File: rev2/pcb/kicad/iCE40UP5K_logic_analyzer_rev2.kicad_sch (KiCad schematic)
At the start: 155 parts, among them IC1 ICE40UP5K-SG48I, IC2 MIC5504-3.3YM5-TR, IC3 MIC5504-1.2YM5-TR, IC4 FT2232HL-TRAY, IC5 W25Q40CLSNIG, IC6 SN74LVC14ADBRE4, IC7 SN74LVC14ADBRE4, IC8 SN74LVC14ADBRE4, J1 USB B Female Connector, J2 61300611121, J3 61202021621, J4 61300821121, J5 61300821121, J6 61300311121, J7 61300621121, Q1 2N7002H6327XTSA2, Y1 830208214809

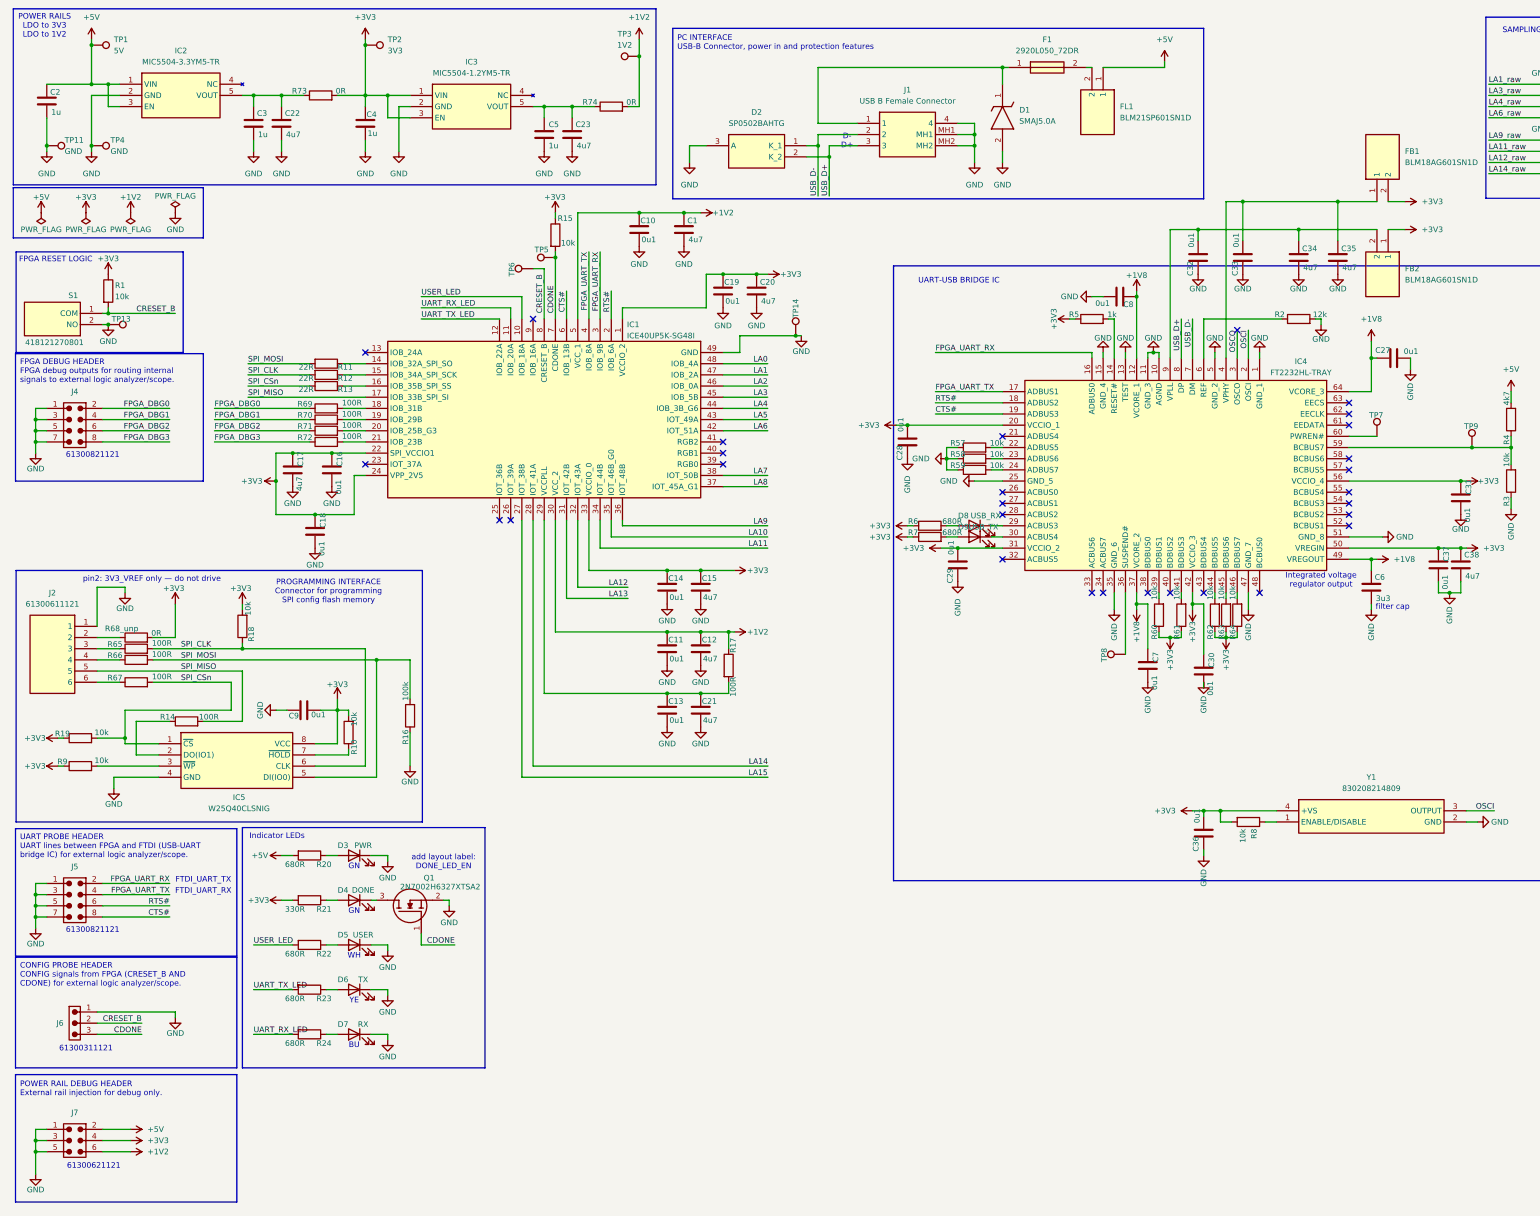
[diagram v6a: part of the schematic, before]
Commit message: reworked schematic test pads. Cleaned up multiple of the schematic blocks.
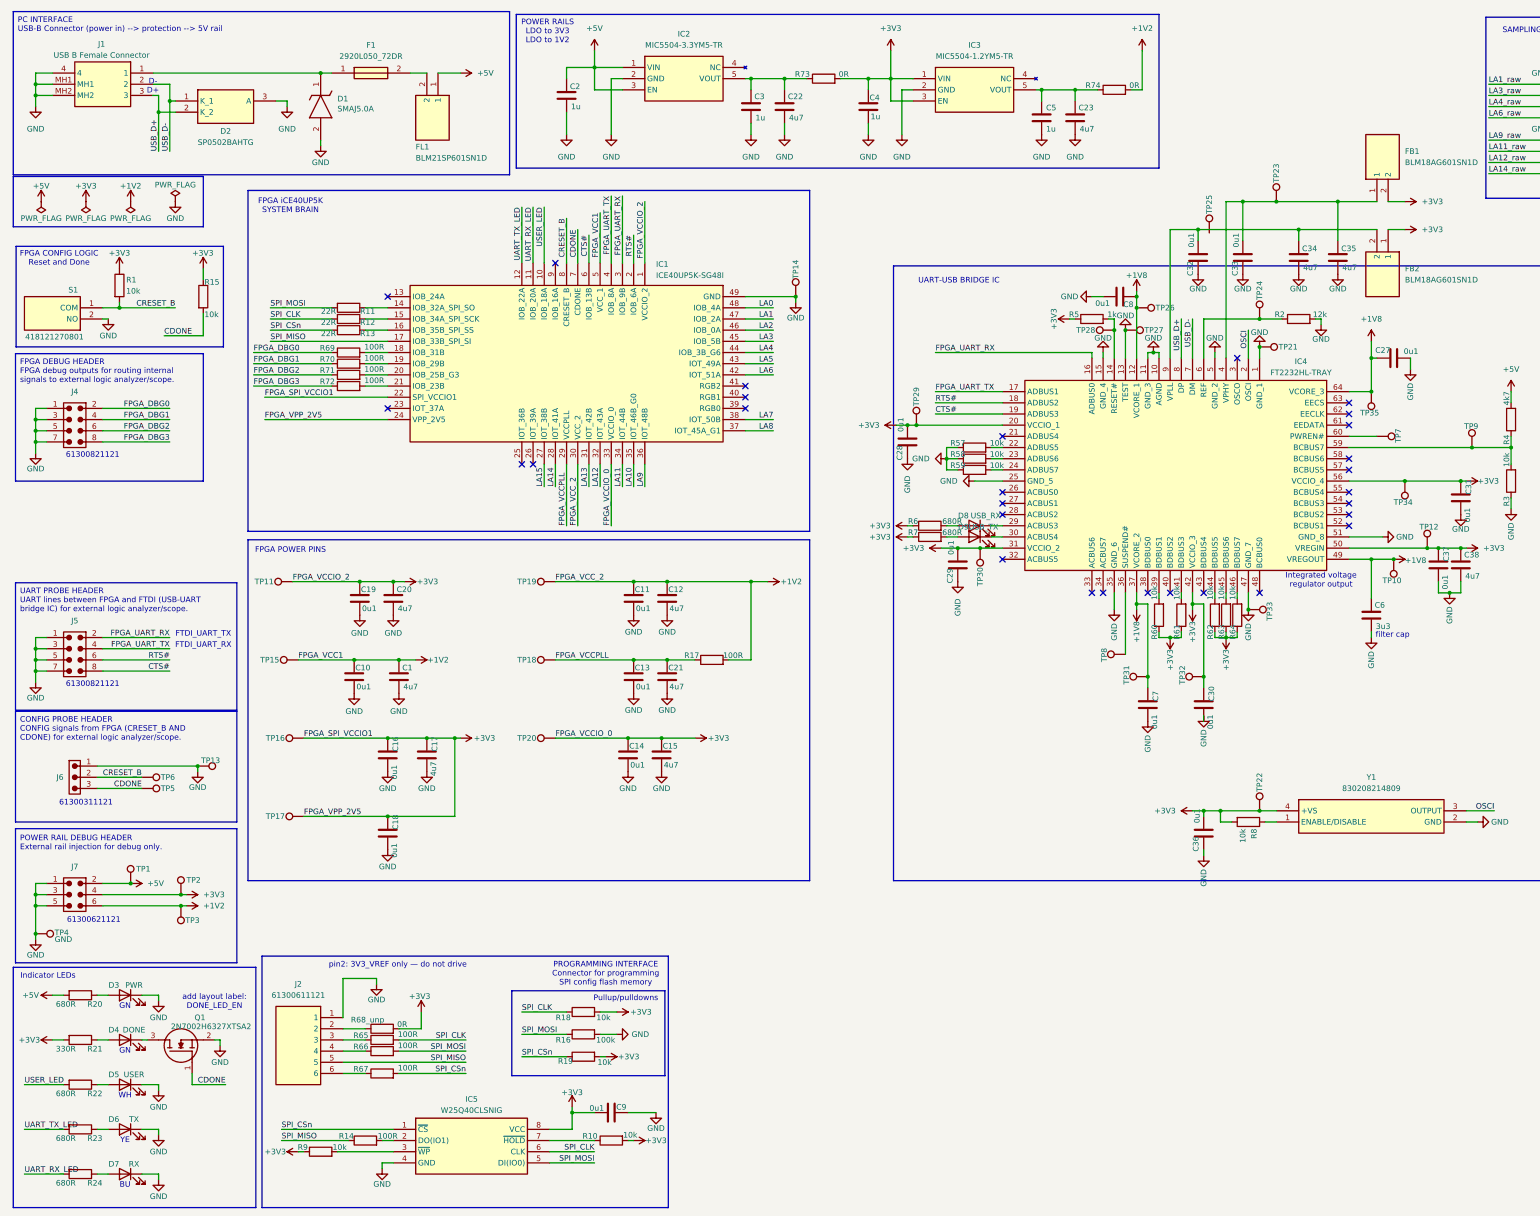
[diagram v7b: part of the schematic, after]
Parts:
- added TP10: VREGOUT, TestPoint:TestPoint_Pad_D1.0mm, symbol Connector:TestPoint
- added TP12: VREGIN, TestPoint:TestPoint_Pad_D1.0mm, symbol Connector:TestPoint
- added TP15: VCC1, TestPoint:TestPoint_Pad_D1.0mm, symbol Connector:TestPoint
- added TP16: SPI_VCCIO1, TestPoint:TestPoint_Pad_D1.0mm, symbol Connector:TestPoint
- added TP17: VPP_2V5, TestPoint:TestPoint_Pad_D1.0mm, symbol Connector:TestPoint
- added TP18: VCC_PLL, TestPoint:TestPoint_Pad_D1.0mm, symbol Connector:TestPoint
- added TP19: VCC_2, TestPoint:TestPoint_Pad_D1.0mm, symbol Connector:TestPoint
- added TP20: VCCIO_0, TestPoint:TestPoint_Pad_D1.0mm, symbol Connector:TestPoint
- added TP21, TP33: GND, TestPoint:TestPoint_Pad_D1.0mm, symbol Connector:TestPoint
- added TP22: VS_OSC, TestPoint:TestPoint_Pad_D1.0mm, symbol Connector:TestPoint
- added TP23: VPHY, TestPoint:TestPoint_Pad_D1.0mm, symbol Connector:TestPoint
- added TP24: REF, TestPoint:TestPoint_Pad_D1.0mm, symbol Connector:TestPoint
- added TP25, TP29, TP30: VPLL, TestPoint:TestPoint_Pad_D1.0mm, symbol Connector:TestPoint
- added TP26: VCORE_1, TestPoint:TestPoint_Pad_D1.0mm, symbol Connector:TestPoint
- added TP27: TEST, TestPoint:TestPoint_Pad_D1.0mm, symbol Connector:TestPoint
- added TP28: RESET#, TestPoint:TestPoint_Pad_D1.0mm, symbol Connector:TestPoint
- added TP31: VCORE_2, TestPoint:TestPoint_Pad_D1.0mm, symbol Connector:TestPoint
- added TP32: VCCIO_3, TestPoint:TestPoint_Pad_D1.0mm, symbol Connector:TestPoint
- added TP34: VCCIO_4, TestPoint:TestPoint_Pad_D1.0mm, symbol Connector:TestPoint
- added TP35: PWREN#, TestPoint:TestPoint_Pad_D1.0mm, symbol Connector:TestPoint
- TP11: value GND -> VCCIO_2; footprint TestPoint:TestPoint_Pad_D1.5mm -> TestPoint:TestPoint_Pad_D1.0mm
- TP7: value BRIDGE_PWREN# -> PWREN#
- TP8: value BRIDGE_SUSPEND# -> SUSPEND#
- TP9: value BRIDGE_PWRSAV# -> PWRSAV#
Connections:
- net +1V2: now also R17.2, TP15.1, TP19.1; no longer R17.1
- net +1V8: now also TP10.1, TP26.1, TP31.1, TP35.1
- net +3V3: now also R19.2, TP11.1, TP12.1, TP16.1, TP17.1, TP20.1, TP22.1, TP29.1, TP30.1, TP32.1, TP34.1; no longer R19.1
- net GND: now also R16.2, TP21.1, TP27.1, TP33.1; no longer R16.1, TP11.1
- net LA14: now also IC1.28 (IOT_41A)
- net LA15: now also IC1.27 (IOT_38B)
- net SPI_CSn: now also R19.1; no longer R19.2
- net SPI_MISO: now also R14.1; no longer R14.2
- net SPI_MOSI: now also R16.1; no longer R16.2
- net FPGA_VCCPLL: now reaches C13.1, C21.1, IC1.29 (VCCPLL)
- net FPGA_VCCPLL: now also R17.1, TP18.1; no longer R17.2
- net at IC4.14 (RESET#), R5.2: now also TP28.1
- net at C33.2, C35.1, FB1.1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: now also TP23.1
- net at IC4.6 (REF), R2.1: now also TP24.1
- net at IC5.2 (DO(IO1)): now also R14.2; no longer R14.1
- net OSCO: no longer names the net of IC4.3 (OSCO)
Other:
- note added: "FPGA CONFIG LOGIC Reset and Done"
- note added: "FPGA POWER PINS"
- note added: "FPGA iCE40UP5K SYSTEM BRAIN"
- note added: "PC INTERFACE USB-B Connector (power in) --> protection --> 5V rail"
- note added: "Pullup/pulldowns"
- note removed: "FPGA RESET LOGIC"
- note removed: "PC INTERFACE USB-B Connector, power in and protection features"
- moved on the sheet: C1, C10, C11, C12, C13, C14, C15, C16, C17, C18, C19, C2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

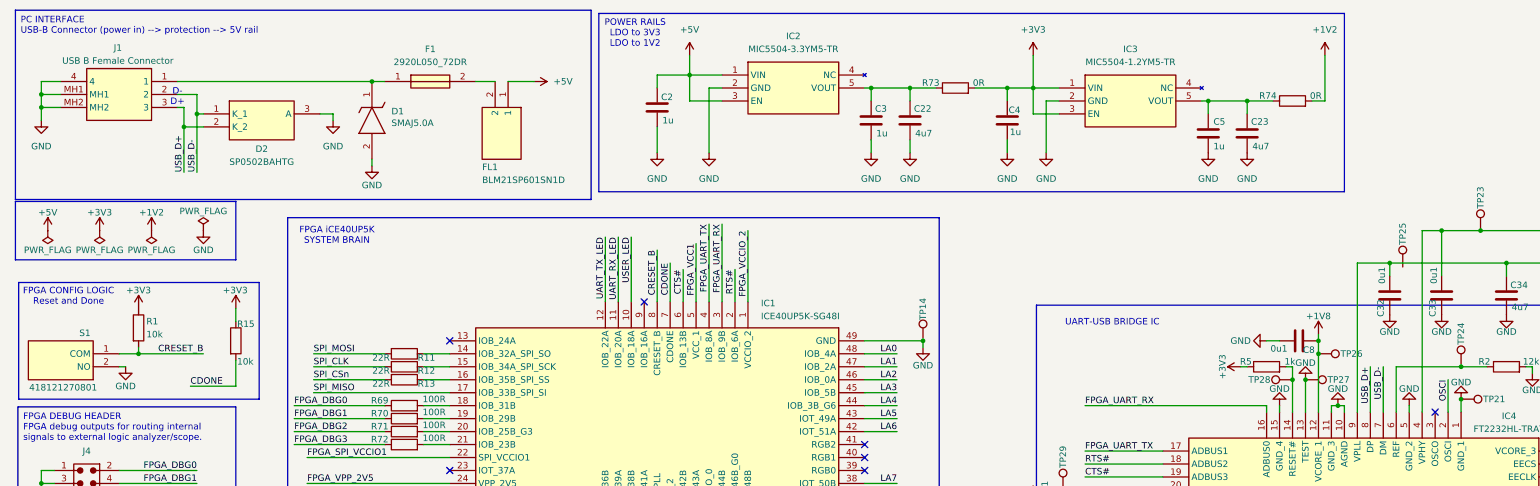
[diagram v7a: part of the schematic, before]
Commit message: CRESET_B slide switch implemented in schematic.
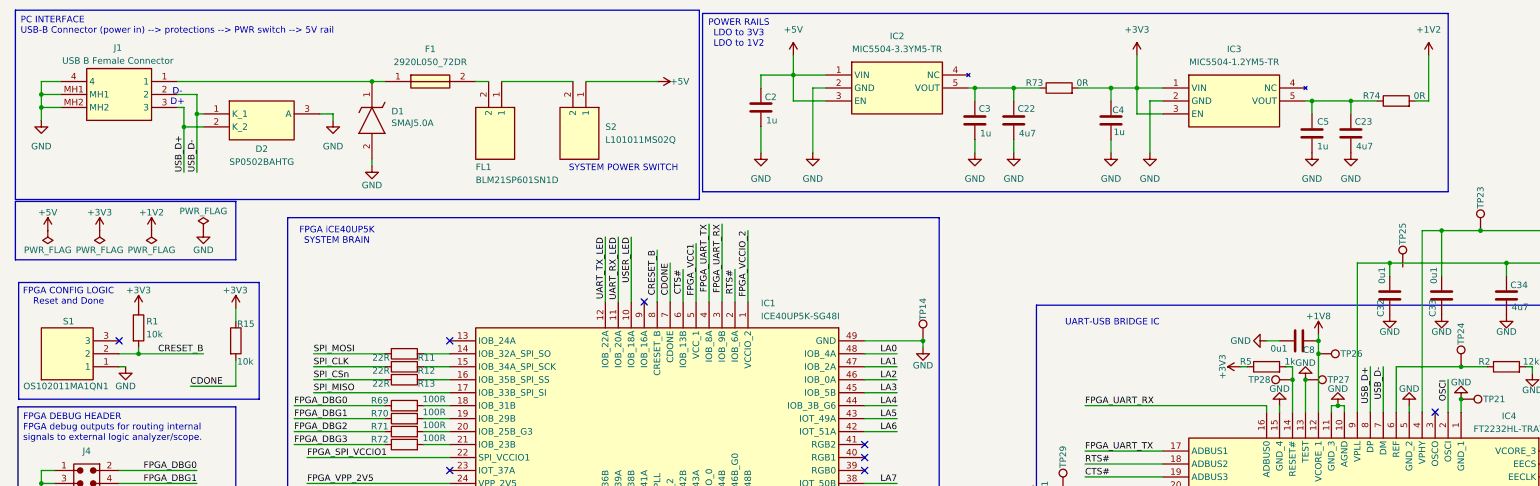
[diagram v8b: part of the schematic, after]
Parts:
- removed S1: 418121270801, 1pole_DIP_switch_418121270801:418121270801, symbol 1pole_DIP_switch_418121270801:418121270801
- added S1: OS102011MA1QN1, OS102011MA1QN1, symbol Slide_switch_SPDT_ON/ON_OS102011MA1QN1:OS102011MA1QN1
- added S2: L101011MS02Q, L101011MS02Q, symbol Slide_switch_SPST_ON/OFF_L101011MS02Q:L101011MS02Q
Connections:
- net +5V: now also S2.1; no longer FL1.1
- net CRESET_B: now also S1.2
- net GND: now also S1.1
- new net: FL1.1, S2.2
- no-connect marks 29 -> 30
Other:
- note added: "PC INTERFACE USB-B Connector (power in) --> protections --> PWR switch --> 5V rail"
- note added: "SYSTEM POWER SWITCH"
- note removed: "PC INTERFACE USB-B Connector (power in) --> protection --> 5V rail"
- moved on the sheet: C2, C22, C23, C3, C4, C5, FL1, IC2, IC3, R73, R74
